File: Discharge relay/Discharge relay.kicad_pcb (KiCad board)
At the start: 2 copper layers, 70 x 85 mm, 8 parts, among them J1 Conn_01x02_MountingPin, J2 Conn_01x02_MountingPin, J3 Conn_01x02_MountingPin, J4 Conn_01x03_MountingPin, K1 NCZ5NE-20F/C11/12

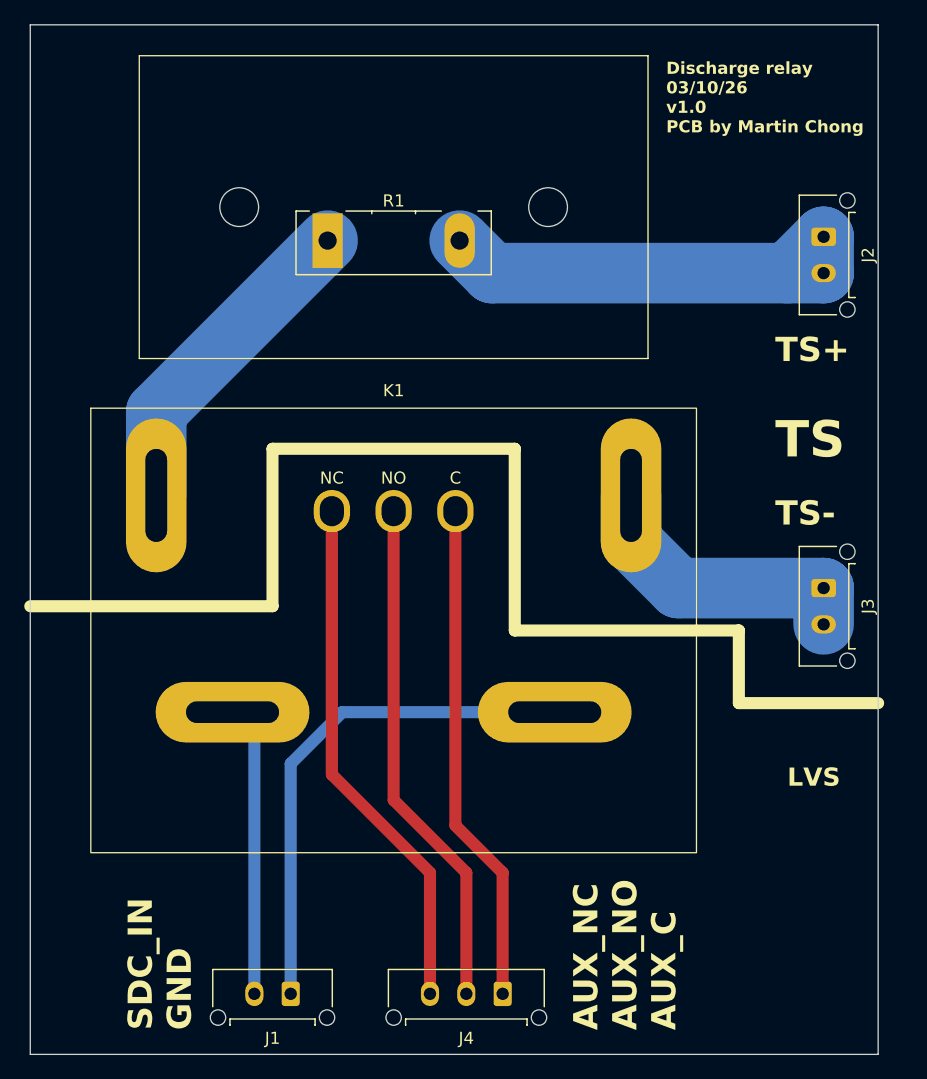
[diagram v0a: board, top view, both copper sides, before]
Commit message: BDUCU, Discharge relay silkscreen change
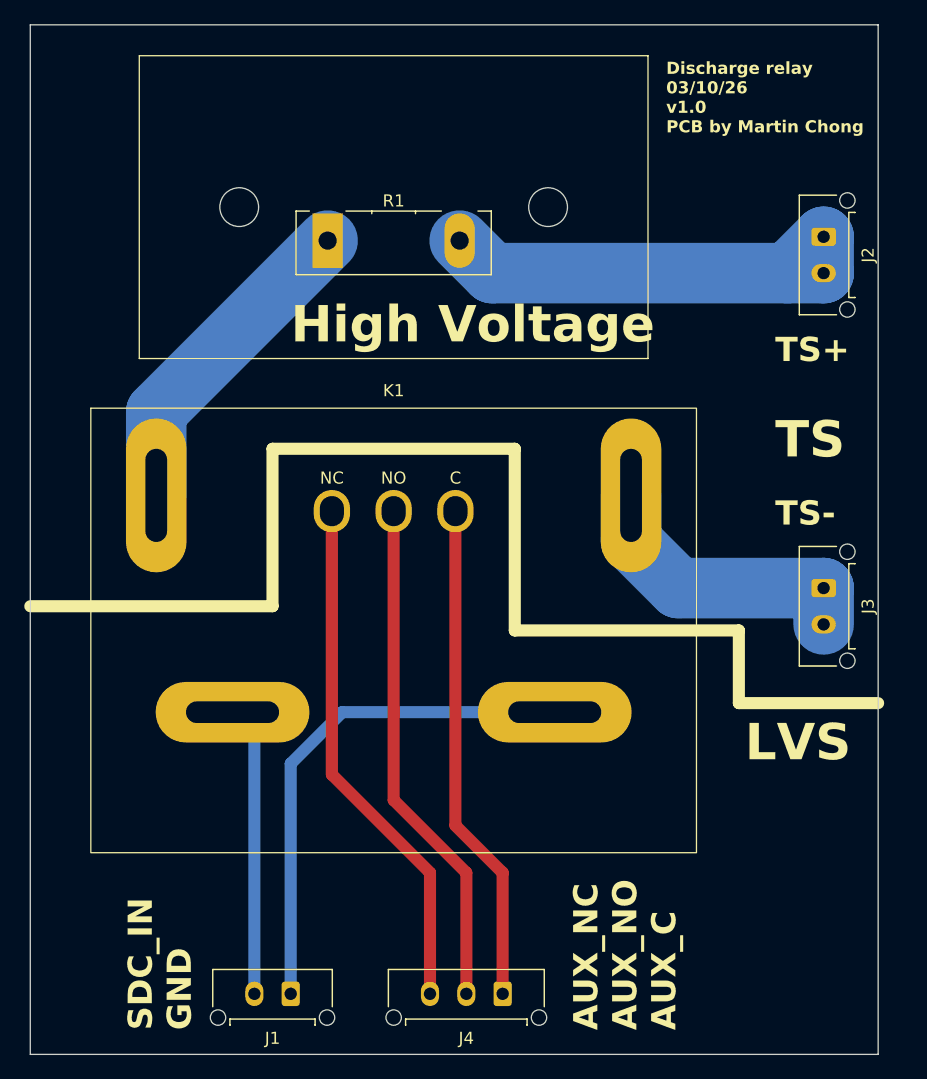
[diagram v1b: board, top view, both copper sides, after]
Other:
- board text added: "High Voltage"
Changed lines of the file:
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@@
 		(layer "F.Cu")
 		(at 75 75)
-		(property "Datasheet" ""
-			(at 0 0 0)
+		(property "Reference" "K1"
+			(at 0 -19.8 0)
 			(unlocked yes)
-			(layer "F.Fab")
-			(hide yes)
+			(layer "F.SilkS")
 			(effects
 				(font
 					(size 1 1)
-					(thickness 0.15)
+					(thickness 0.1)
 				)
 			)
 		)
-		(property "Description" "Relay SPST, normally open, EN50005"
-			(at 0 0 0)
+		(property "Value" "NCZ5NE-20F/C11/12"
+			(at 0 1 0)
 			(unlocked yes)
 			(layer "F.Fab")
-			(hide yes)
 			(effects
 				(font
@@
 			)
 		)
-		(property "Value" "NCZ5NE-20F/C11/12"
-			(at 0 1 0)
+		(property "Datasheet" ""
+			(at 0 0 0)
 			(unlocked yes)
 			(layer "F.Fab")
+			(hide yes)
 			(effects
 				(font
@@
 			)
 		)
-		(property "Reference" "K1"
-			(at 0 -19.8 0)
+		(property "Description" "Relay SPST, normally open, EN50005"
+			(at 0 0 0)
 			(unlocked yes)
-			(layer "F.SilkS")
+			(layer "F.Fab")
+			(hide yes)
 			(effects
 				(font
 					(size 1 1)
-					(thickness 0.1)
+					(thickness 0.15)
 				)
 			)
@@
 		(start 45 25)
 		(end 115 110)
+		(radius 5)
 		(stroke
 			(width 0.1)
@@
 		)
 	)
-	(gr_text "LVS"
-		(at 107.5 88 0)
-		(layer "F.SilkS")
-		(effects
-			(font
-				(size 1.5 1.5)
-				(thickness 0.3)
-				(bold yes)
-			)
-			(justify left bottom)
-		)
-	)
 	(gr_text "TS+"
 		(at 106.5 53 0)
@@
 		)
 	)
-	(gr_text "TS"
-		(at 106.5 61 0)
+	(gr_text "High Voltage"
+		(at 66.5 51.5 0)
 		(layer "F.SilkS")
 		(effects
@@
 		)
 	)
-	(segment
-		(start 63.5 105)
-		(end 63.5 81.75)
-		(width 1)
-		(layer "B.Cu")
-		(net "SDC_IN")
+	(gr_text "LVS"
+		(at 104 86 0)
+		(layer "F.SilkS")
+		(effects
+			(font
+				(size 3 3)
+				(thickness 0.6)
+				(bold yes)
+			)
+			(justify left bottom)
+		)
 	)
-	(segment
-		(start 63.5 81.75)
-		(end 61.7 81.75)
-		(width 1)
-		(layer "B.Cu")
-		(net "SDC_IN")
+	(gr_text "TS"
+		(at 106.5 61 0)
+		(layer "F.SilkS")
+		(effects
+			(font
+				(size 3 3)
+				(thickness 0.6)
+				(bold yes)
+			)
+			(justify left bottom)
+		)
 	)
 	(segment
@@
 	)
 	(segment
+		(start 63.5 105)
+		(end 63.5 81.75)
+		(width 1)
+		(layer "B.Cu")
+		(net "SDC_IN")
+	)
+	(segment
+		(start 63.5 81.75)
+		(end 61.7 81.75)
+		(width 1)
+		(layer "B.Cu")
+		(net "SDC_IN")
+	)
+	(segment
 		(start 66.5 105)
 		(end 66.5 86)
@@
 	)
 	(segment
-		(start 80.45 42.815)
-		(end 83.135 45.5)
-		(width 5)
-		(layer "B.Cu")
-		(net "TS+")
-	)
-	(segment
-		(start 110.5 42.5)
-		(end 107.5 45.5)
-		(width 5)
-		(layer "B.Cu")
-		(net "TS+")
-	)
-	(segment
-		(start 110.5 42.5)
-		(end 110.5 45.5)
-		(width 5)
-		(layer "B.Cu")
-		(net "TS+")
-	)
-	(segment
-		(start 83.135 45.5)
-		(end 110.5 45.5)
-		(width 5)
-		(layer "B.Cu")
-		(net "TS+")
-	)
-	(segment
-		(start 80.1 91.1)
-		(end 80.1 65.15)
+		(start 81 95)
+		(end 75 89)
 		(width 1)
 		(layer "F.Cu")
-		(net "AUX_C")
+		(net "AUX_NO")
 	)
 	(segment
-		(start 84 105)
-		(end 84 95)
+		(start 81 105)
+		(end 81 95)
 		(width 1)
 		(layer "F.Cu")
-		(net "AUX_C")
+		(net "AUX_NO")
 	)
 	(segment
-		(start 84 95)
-		(end 80.1 91.1)
+		(start 75 89)
+		(end 75 65.15)
 		(width 1)
 		(layer "F.Cu")
-		(net "AUX_C")
+		(net "AUX_NO")
 	)
 	(segment
@@
 	)
 	(segment
-		(start 81 95)
-		(end 75 89)
+		(start 80.1 91.1)
+		(end 80.1 65.15)
 		(width 1)
 		(layer "F.Cu")
-		(net "AUX_NO")
+		(net "AUX_C")
 	)
 	(segment
-		(start 81 105)
-		(end 81 95)
+		(start 84 105)
+		(end 84 95)
 		(width 1)
 		(layer "F.Cu")
-		(net "AUX_NO")
+		(net "AUX_C")
 	)
 	(segment
-		(start 75 89)
-		(end 75 65.15)
+		(start 84 95)
+		(end 80.1 91.1)
 		(width 1)
 		(layer "F.Cu")
-		(net "AUX_NO")
+		(net "AUX_C")
+	)
+	(segment
+		(start 80.45 42.815)
+		(end 83.135 45.5)
+		(width 5)
+		(layer "B.Cu")
+		(net "TS+")
+	)
+	(segment
+		(start 110.5 42.5)
+		(end 107.5 45.5)
+		(width 5)
+		(layer "B.Cu")
+		(net "TS+")
+	)
+	(segment
+		(start 110.5 42.5)
+		(end 110.5 45.5)
+		(width 5)
+		(layer "B.Cu")
+		(net "TS+")
+	)
+	(segment
+		(start 83.135 45.5)
+		(end 110.5 45.5)
+		(width 5)
+		(layer "B.Cu")
+		(net "TS+")
 	)
 	(embedded_fonts no)
